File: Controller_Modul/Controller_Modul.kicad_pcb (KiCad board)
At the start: 4 copper layers, 78 x 100 mm, 140 parts, among them J101 Screw_Terminal_01x06, J102 Conn_02x01, J103 Conn_01x06_Male, J104 Conn_02x01, J105 Conn_01x04_Male, J106 Conn_01x08_Male, J107 Micro_SD_Card_Det, J108 IPC 16P, J109 Conn_02x20_Odd_Even, J110 USB_B_Mini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

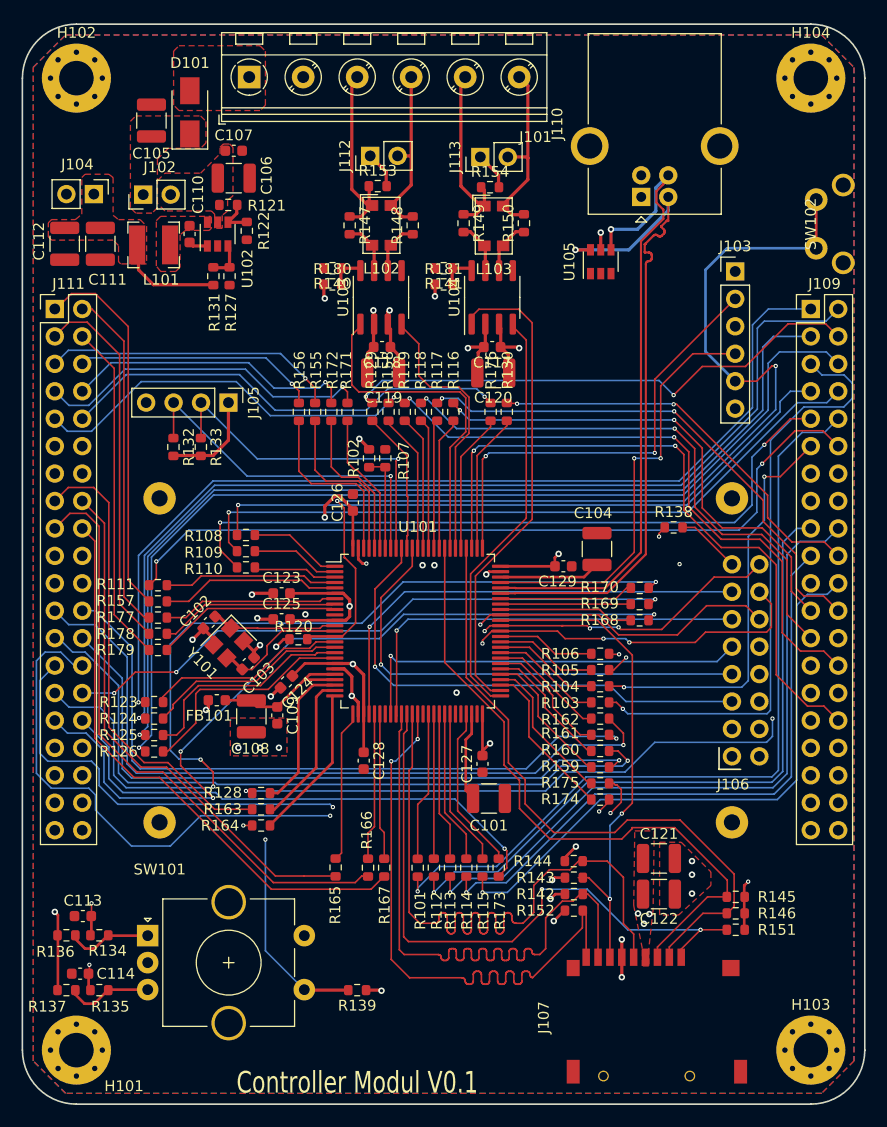
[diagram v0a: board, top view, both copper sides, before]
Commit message: ESD Protection für Feeder Modul USB hinzugefügt, Status LED für Controller Modul hinzugefügt
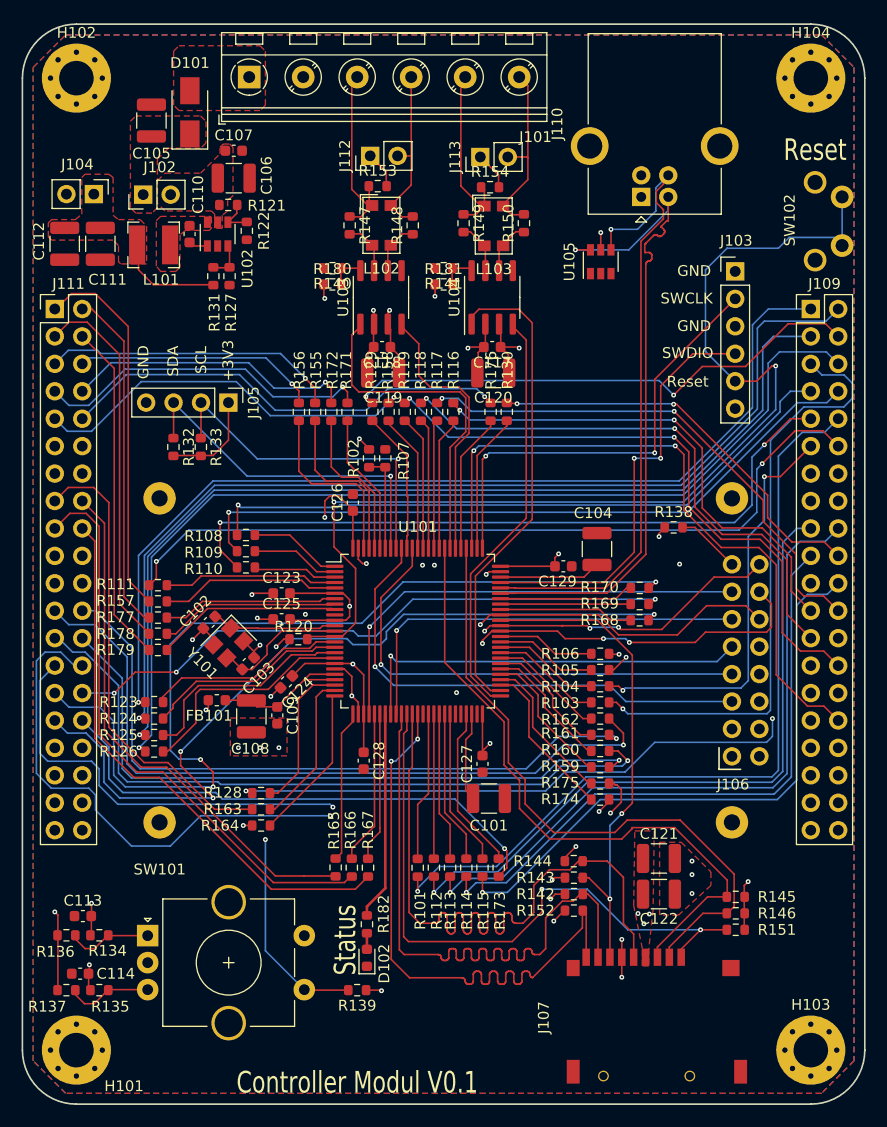
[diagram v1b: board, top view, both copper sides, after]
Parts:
- added D102: LED_Blue, LED_SMD:LED_0603_1608Metric, F.Cu at (111.9, 136.4)
- added R182: 1K, Resistor_SMD:R_0603_1608Metric, F.Cu at (111.9, 133.3)
- moved SW102 2.41 mm to (155.9, 68.2), turned to 90 degrees
- moved R166 1.50 mm to (110.5, 128.1)
- moved R167 1.50 mm to (112.0, 128.1)
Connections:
- U101 pad 32: (no net) -> Net-(R182-Pad1)
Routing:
- net Net-(R182-Pad1): track 0.00 -> 19.4 mm
- net /NRST: track 96.7 -> 100.1 mm
- net /ADC_RES4: track 53.0 -> 51.5 mm
- net /ADC_RES3: track 55.3 -> 53.7 mm
- net Net-(D102-Pad2): track 0.00 -> 1.49 mm
- net /OUTPUT_RES6: track 74.8 -> 75.6 mm
- net /PA5: track 13.5 -> 14.1 mm
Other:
- net class Default: via_dia 0.8 -> 0.45; via_drill 0.4 -> 0.2
- net class USB_90Ohm: via_dia 0.4 -> 0.45
- board text added: "+3V3"
- board text added: "GND"
- board text added: "Reset"
- board text added: "SCL"
- board text added: "SDA"
- board text added: "SWCLK"
- board text added: "SWDIO"
- board text added: "Status"

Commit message: Fiducials auf allen Boards hinzugefügt
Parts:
- added FID101: Fiducial, Fiducial:Fiducial_1mm_Mask2mm, F.Cu at (85.0, 61.0)
- added FID102: Fiducial, Fiducial:Fiducial_1mm_Mask2mm, F.Cu at (85.0, 129.0)
- added FID103: Fiducial, Fiducial:Fiducial_1mm_Mask2mm, F.Cu at (153.0, 129.0)

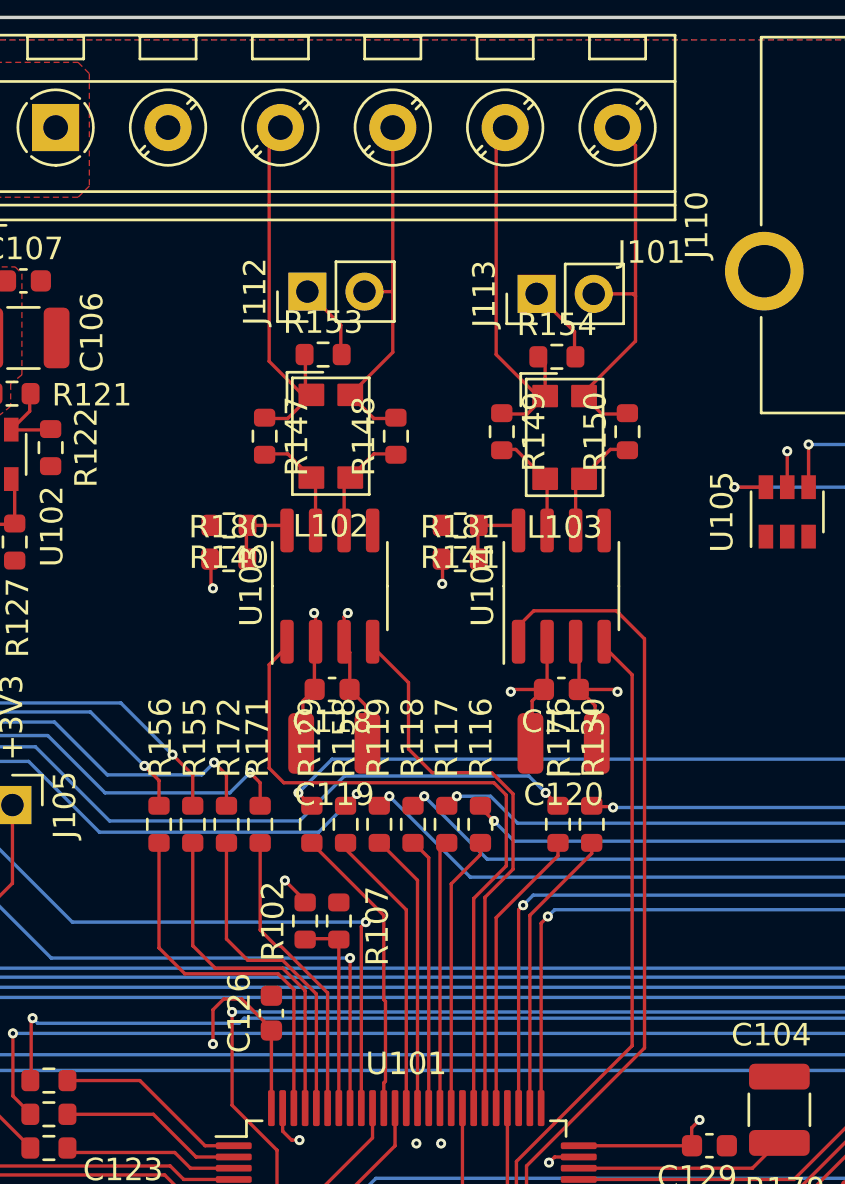
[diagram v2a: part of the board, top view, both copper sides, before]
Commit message: ESD Protection überarbeitet, aber noch nicht fertig
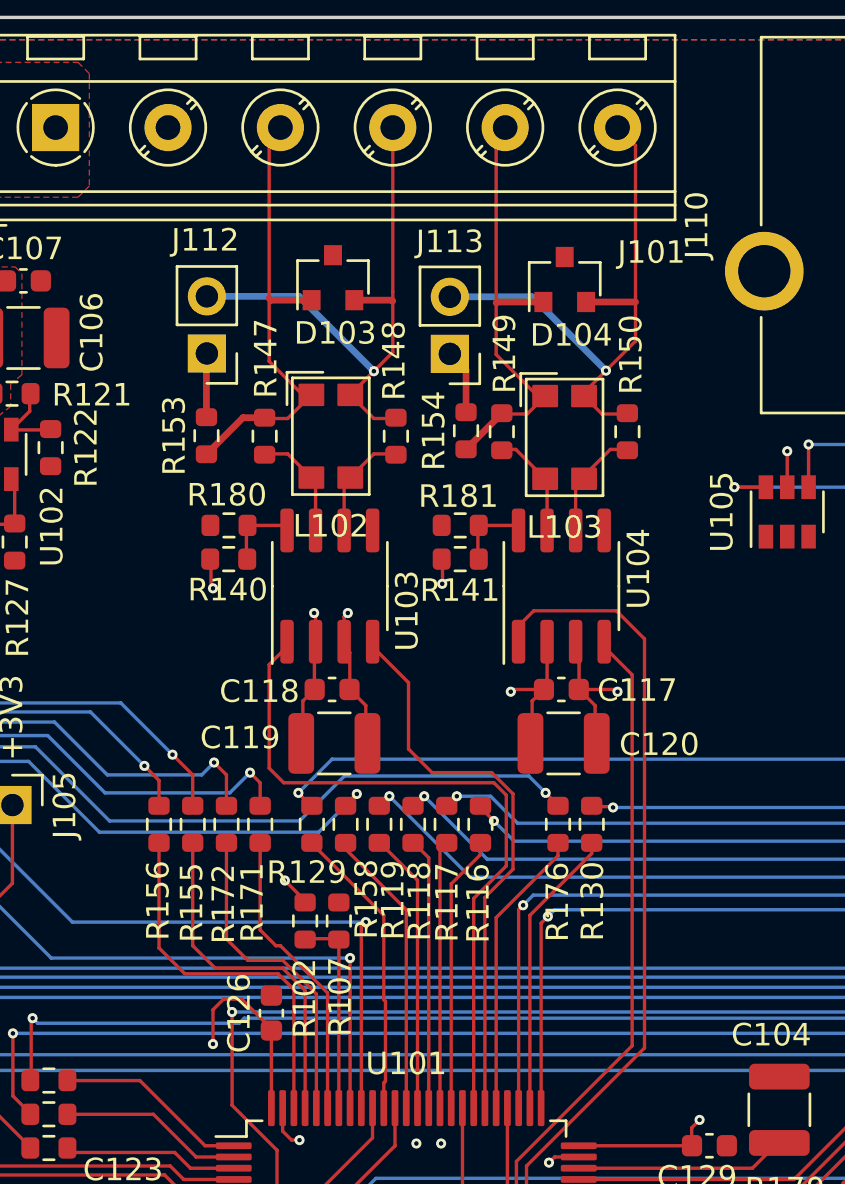
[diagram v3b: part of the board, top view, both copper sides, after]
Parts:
- added D103: SM24CANA-02HTG, Package_TO_SOT_SMD:SOT-23, F.Cu at (113.3, 61.6)
- added D104: SM24CANA-02HTG, Package_TO_SOT_SMD:SOT-23, F.Cu at (123.7, 61.7)
- moved R153 6.32 mm to (107.7, 68.6), turned to 90 degrees
- moved J112 5.25 mm to (107.7, 65.0), turned to 180 degrees
- moved R154 5.21 mm to (119.3, 68.4), turned to 90 degrees
- moved J113 4.69 mm to (118.5, 65.0), turned to 180 degrees
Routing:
- net /CAN1_L: track 16.4 -> 25.7 mm, vias 0 -> 1
- net /CAN2_L: track 17.4 -> 26.0 mm, vias 0 -> 1
- net /CAN1_H: track 17.5 -> 21.2 mm
- net /CAN2_H: track 17.3 -> 19.9 mm
- net Net-(J113-Pad1): track 3.50 -> 2.89 mm
- net Net-(J112-Pad1): track 3.42 -> 2.84 mm

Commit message: Änderungen für bestellung V01 -  Bestellung abgeschickt
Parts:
- moved U105 4.48 mm to (138.0, 71.4)
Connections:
- U105 pad 4: /USB_FS_D+ -> /USB_FS_D-
- U105 pad 6: /USB_FS_D- -> /USB_FS_D+
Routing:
- net /USB_FS_D-: track 63.2 -> 52.3 mm, vias 1 -> 0
- net /USB_FS_D+: track 61.2 -> 52.2 mm, vias 1 -> 0
- net +3V3: track 96.3 -> 95.7 mm
